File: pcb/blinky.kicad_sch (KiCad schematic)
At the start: 13 parts, among them U1 ATtiny13A-SS

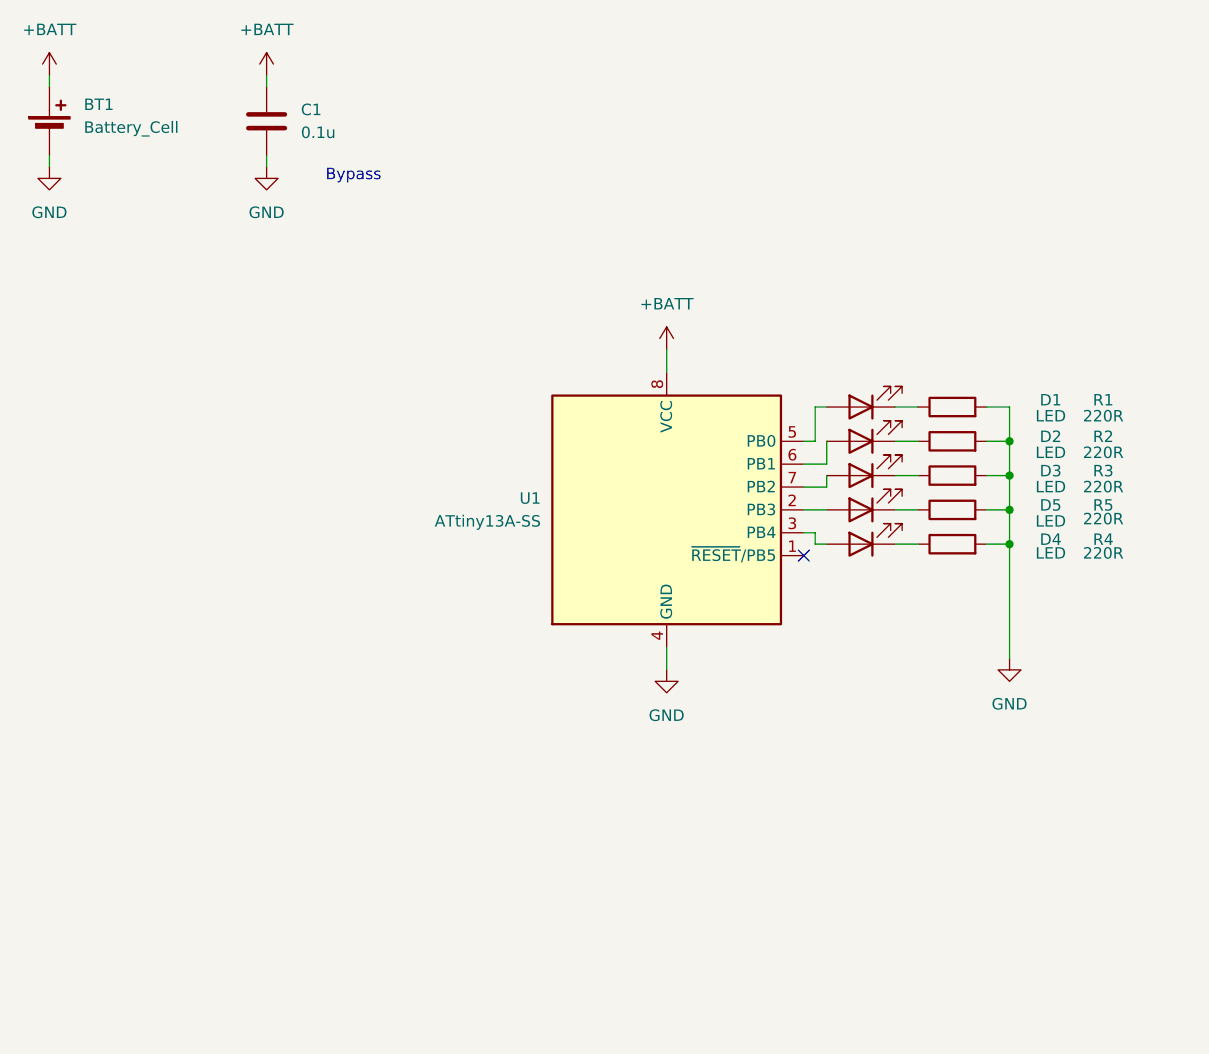
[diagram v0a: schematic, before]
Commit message: Add ISP header and LCSC part no.
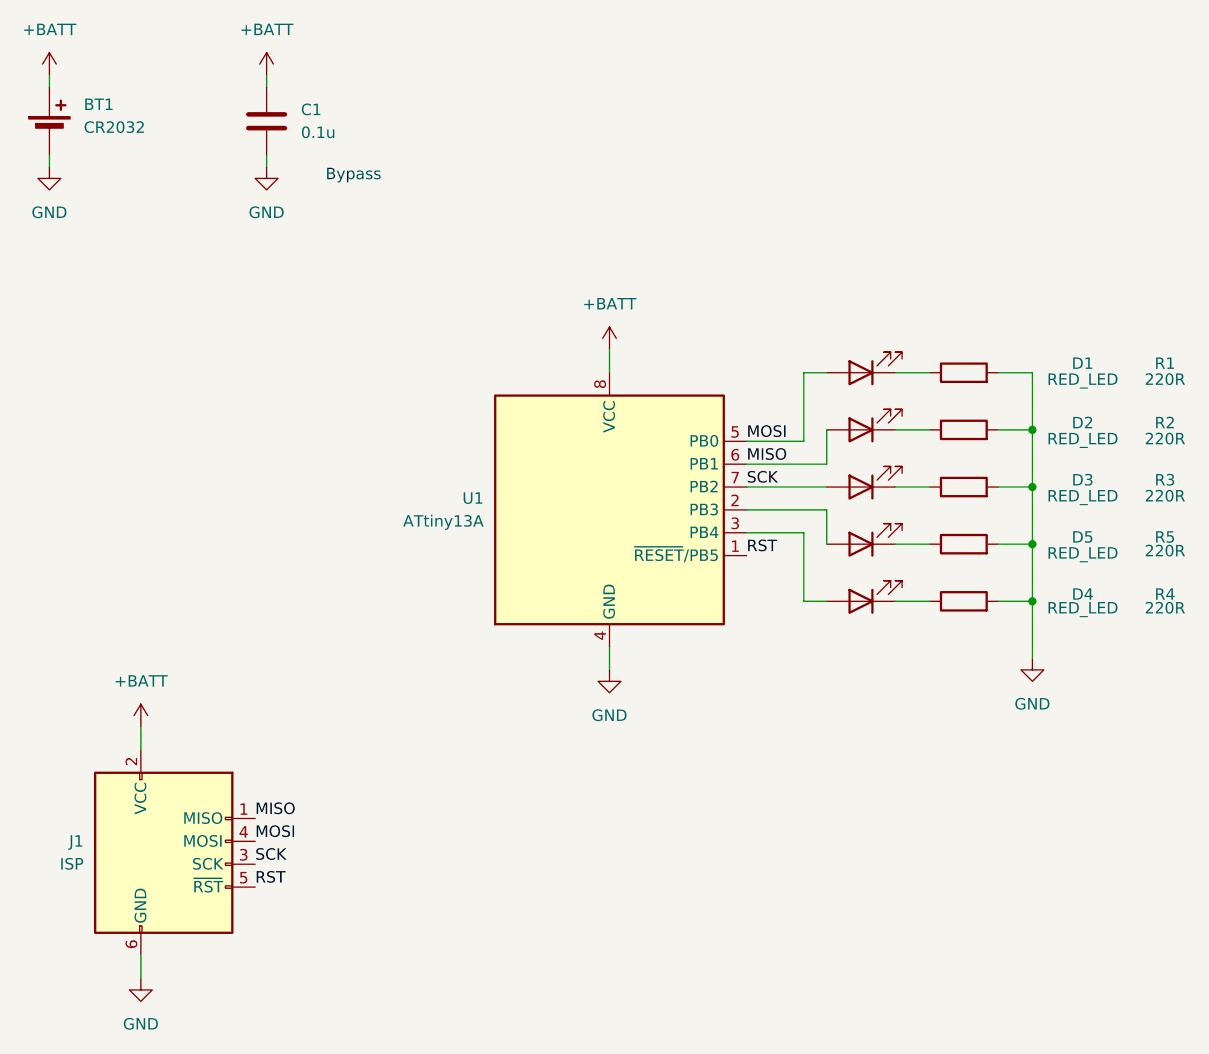
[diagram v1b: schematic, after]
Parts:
- added J1: ISP, JTAG:06x1_1.27mm, symbol Connector:AVR-ISP-6
- BT1: value Battery_Cell -> CR2032; LCSC (none) -> C70373
- C1: LCSC (none) -> C476766
- D1, D2, D3, D4, D5: value LED -> RED_LED; LCSC (none) -> C965812
- R1, R2, R3, R4, R5: LCSC (none) -> C2933537
- U1: value ATtiny13A-SS -> ATtiny13A; LCSC (none) -> C40382
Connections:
- net +BATT: now also J1.2 (VCC)
- net GND: now also J1.6 (GND)
- net MOSI: now reaches D1.2 (A), U1.5 (PB0)
- net MOSI: now also J1.4 (MOSI)
- net MISO: now reaches D2.2 (A), U1.6 (PB1)
- net MISO: now also J1.1 (MISO)
- net SCK: now reaches D3.2 (A), U1.7 (PB2)
- net SCK: now also J1.3 (SCK)
- net RST: now reaches U1.1 (~{RESET}/PB5)
- net RST: now also J1.5 (~{RST})
- no-connect marks 1 -> 0
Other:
- moved on the sheet: D1, D2, D3, D4, D5, R1, R2, R3, R4, R5, U1
